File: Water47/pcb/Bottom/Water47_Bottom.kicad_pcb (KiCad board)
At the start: 2 copper layers, 260 x 76.5 mm, 11 parts

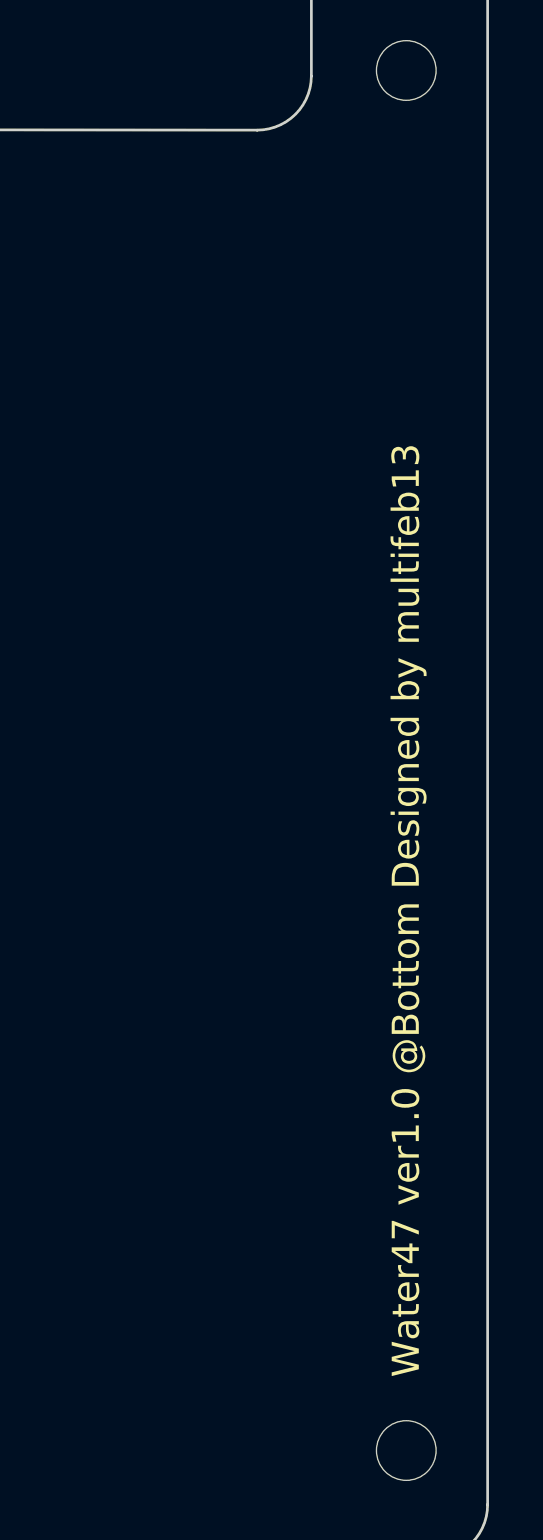
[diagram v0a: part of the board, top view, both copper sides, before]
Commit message: fix: invisible redundant silkscreen
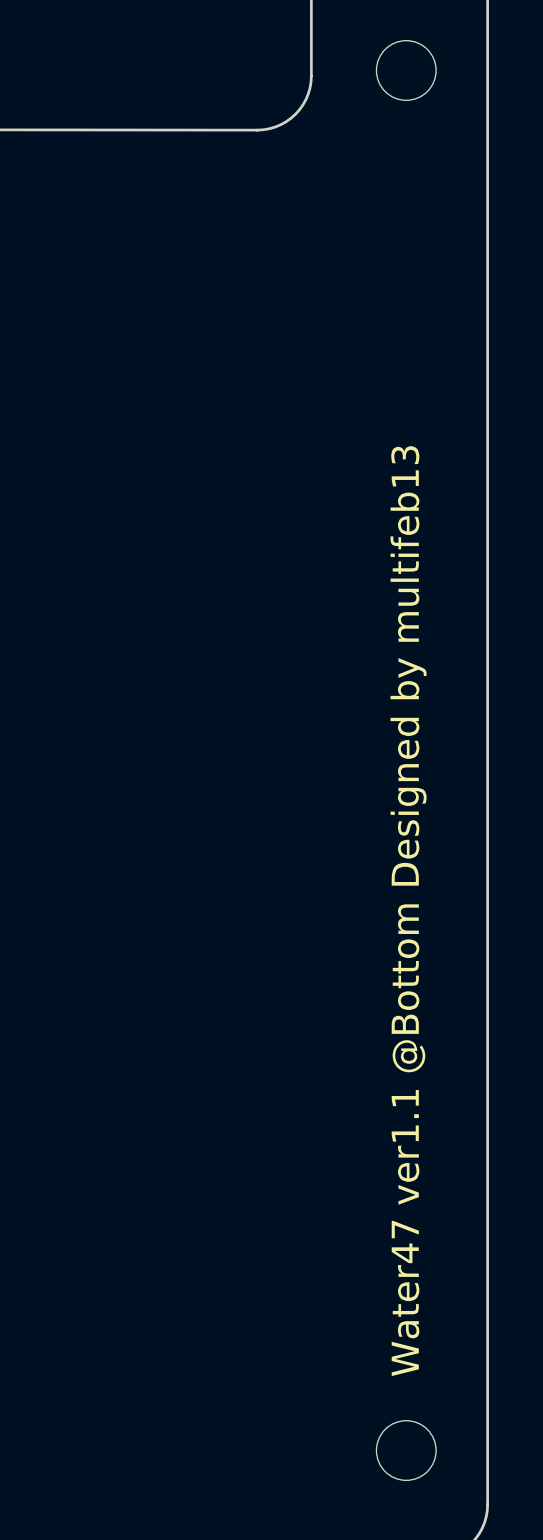
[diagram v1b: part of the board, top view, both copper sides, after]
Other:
- board text added: "Water47 ver1.1 @Bottom Designed by multifeb13"
- board text removed: "Water47 ver1.0 @Bottom Designed by multifeb13"
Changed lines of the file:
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@@
     (at 212 121.45 180)
     (attr board_only exclude_from_pos_files exclude_from_bom)
-    (fp_text reference "G***" (at 0 0) (layer "B.SilkS")
+    (fp_text reference "G***" (at 0 0) (layer "B.SilkS") hide
       (effects (font (size 1.524 1.524) (thickness 0.3)) (justify mirror))
     )
@@
   (gr_arc (start 319 106.985786) (mid 317.585786 106.4) (end 317 104.985786) (layer "Edge.Cuts") (width 0.1))
   (gr_arc (start 84 159.7) (mid 82.585786 159.114214) (end 82 157.7) (layer "Edge.Cuts") (width 0.1))
-  (gr_text "Water47 ver1.0 @Bottom Designed by multifeb13" (at 339 153 90) (layer "F.SilkS")
+  (gr_text "Water47 ver1.1 @Bottom Designed by multifeb13" (at 339 153 90) (layer "F.SilkS")
     (effects (font (size 1 1) (thickness 0.125)) (justify left))
   )
